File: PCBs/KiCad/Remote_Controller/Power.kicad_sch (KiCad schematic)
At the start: 20 parts

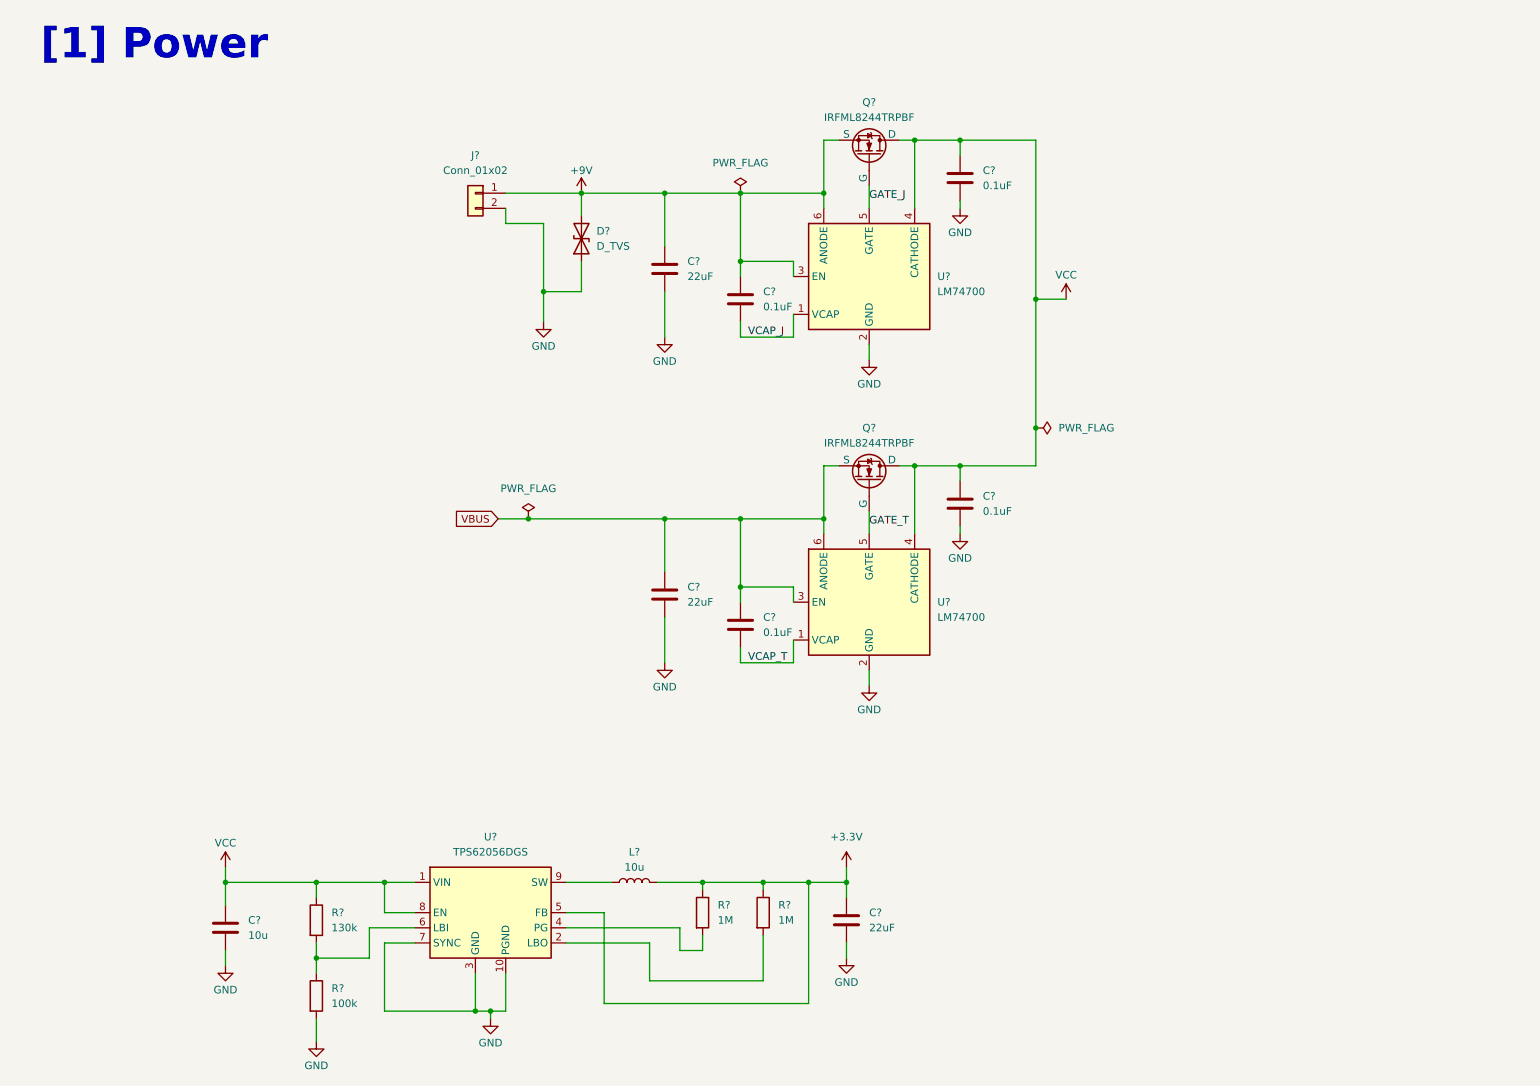
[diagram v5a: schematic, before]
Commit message: Finish power schematic, 3.3V buck converter and 3V LDO
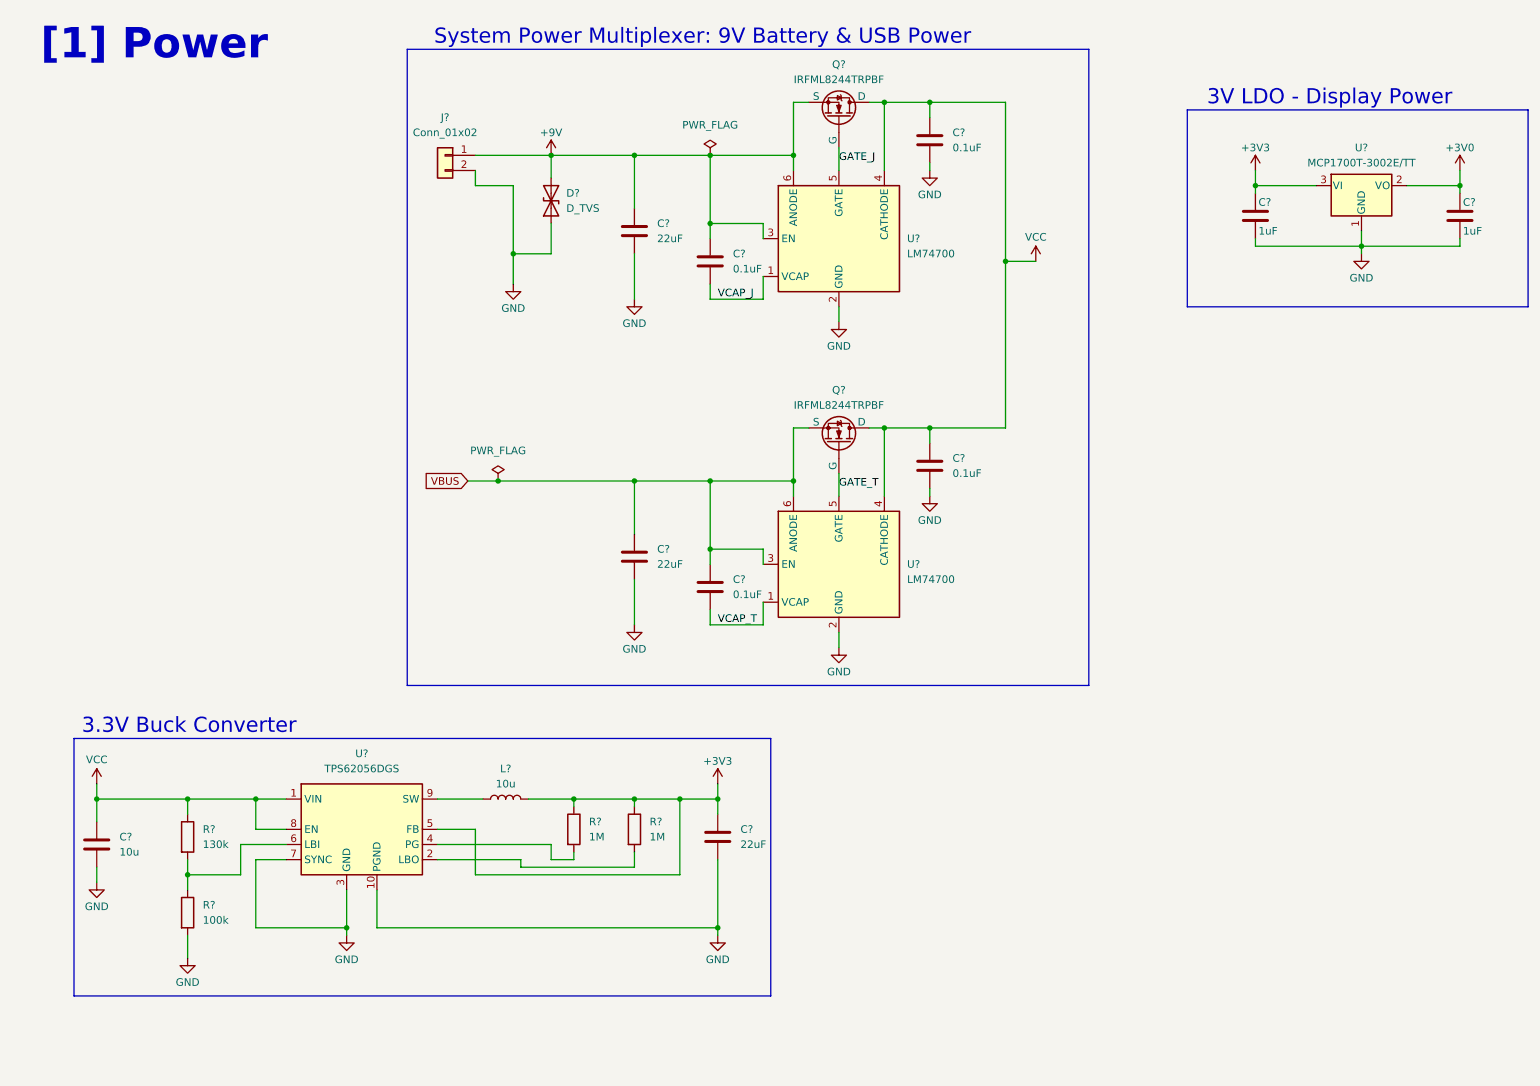
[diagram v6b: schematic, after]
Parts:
- added C? (x2): 1uF, Capacitor_SMD:C_0402_1005Metric, symbol Device:C
- added U?: MCP1700T-3002E/TT, Package_TO_SOT_SMD:SOT-23, symbol Regulator_Linear:MCP1700x-300xxTT
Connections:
- net GND: now also C?.2, C?.2, U?.1 (GND)
- net +3.3V renamed +3V3
- net +3V3: now also C?.1, U?.3 (VI)
- new net +3V0: C?.1, U?.2 (VO)
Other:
- note added: "3.3V Buck Converter"
- note added: "3V LDO - Display Power"
- note added: "System Power Multiplexer: 9V Battery & USB Power"
- moved on the sheet: C?, D?, J?, L?, Q?, R?, U?

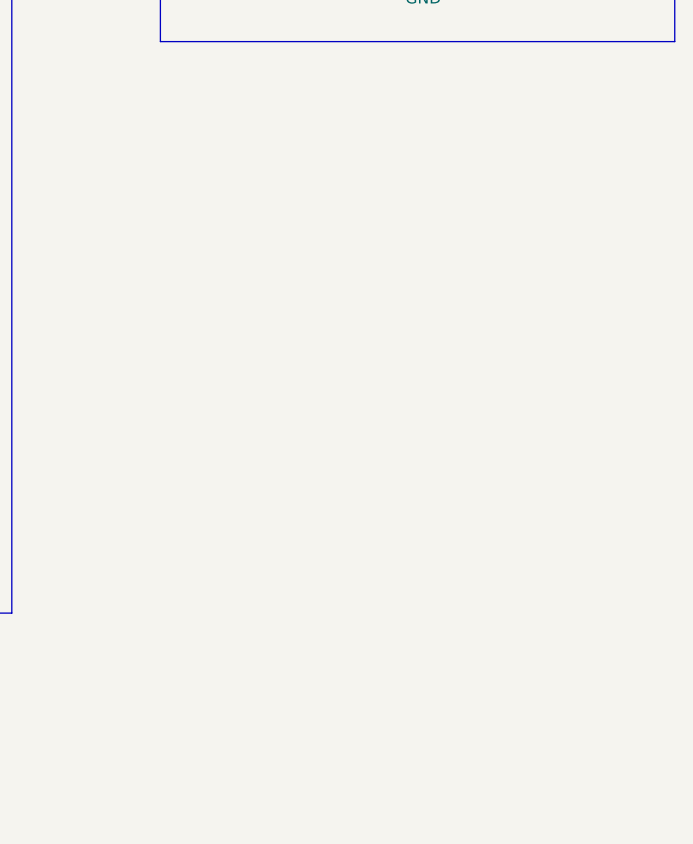
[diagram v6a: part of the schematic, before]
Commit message: Add Power on indicator light, made small corrections
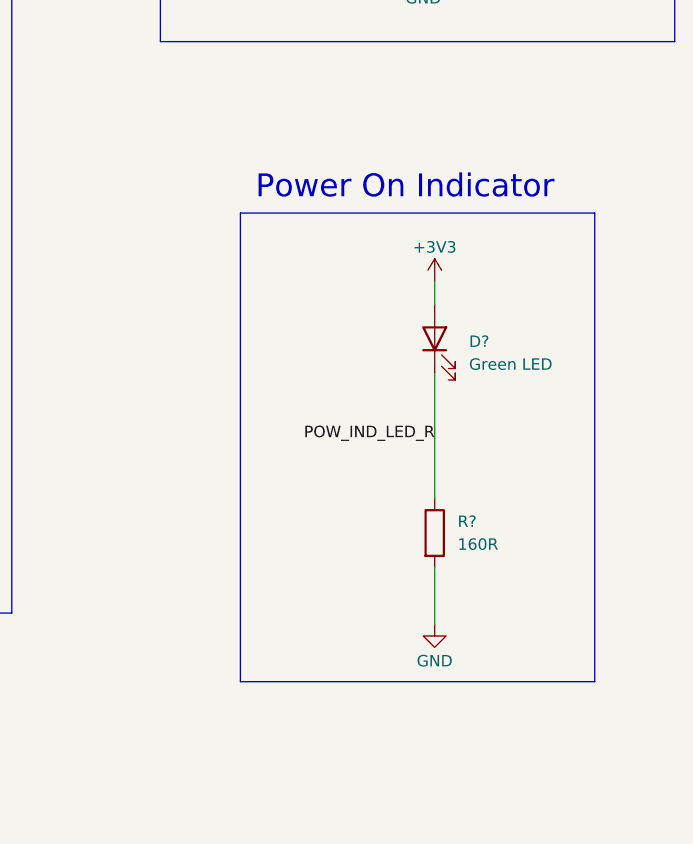
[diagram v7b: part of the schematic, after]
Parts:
- added D?: Green LED, LED_SMD:LED_0603_1608Metric, symbol Device:LED
- added R?: 160R, Resistor_SMD:R_0603_1608Metric, symbol Device:R
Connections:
- net +3V3: now also D?.2 (A)
- net GND: now also R?.2
- new net POW_IND_LED_R: D?.1 (K), R?.1
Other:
- note added: "Power On Indicator"

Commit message: Add power switch
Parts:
- added SW?: Power Switch, symbol Switch:SW_SPST
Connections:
- net +9V: now also SW?.1 (A); no longer C?.1, C?.1, Q?.2 (S), U?.3 (EN), U?.6 (ANODE)
- new net: C?.1, C?.1, Q?.2 (S), SW?.2 (B), U?.3 (EN), U?.6 (ANODE)
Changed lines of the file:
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@@
 	(paper "A4")
 	(junction
-		(at 130.81 170.18)
+		(at 116.84 40.64)
 		(diameter 0)
 		(color 0 0 0 0)
 	)
 	(junction
-		(at 26.67 148.59)
+		(at 130.81 170.18)
 		(diameter 0)
 		(color 0 0 0 0)
 	)
 	(junction
-		(at 143.51 40.64)
+		(at 26.67 148.59)
 		(diameter 0)
 		(color 0 0 0 0)
 	)
 	(junction
-		(at 238.76 55.88)
+		(at 143.51 40.64)
 		(diameter 0)
 		(color 0 0 0 0)
 	)
 	(junction
-		(at 116.84 40.64)
+		(at 238.76 55.88)
 		(diameter 0)
 		(color 0 0 0 0)
@@
 	)
 	(junction
-		(at 102.87 40.64)
-		(diameter 0)
-		(color 0 0 0 0)
-	)
-	(junction
 		(at 106.68 148.59)
 		(diameter 0)
@@
 	)
 	(junction
+		(at 96.52 40.64)
+		(diameter 0)
+		(color 0 0 0 0)
+	)
+	(junction
 		(at 116.84 148.59)
 		(diameter 0)
@@
 	)
 	(junction
+		(at 102.87 40.64)
+		(diameter 0)
+		(color 0 0 0 0)
+	)
+	(junction
 		(at 116.84 95.25)
 		(diameter 0)
@@
 	(wire
 		(pts
-			(xy 102.87 40.64) (xy 116.84 40.64)
-		)
-		(stroke
-			(width 0)
-			(type default)
-		)
-	)
-	(wire
-		(pts
 			(xy 41.91 148.59) (xy 53.34 148.59)
 		)
@@
 	(wire
 		(pts
+			(xy 115.57 40.64) (xy 116.84 40.64)
+		)
+		(stroke
+			(width 0)
+			(type default)
+		)
+	)
+	(wire
+		(pts
 			(xy 231.14 45.72) (xy 220.98 45.72)
 		)
@@
 	(wire
 		(pts
-			(xy 90.17 40.64) (xy 102.87 40.64)
+			(xy 90.17 40.64) (xy 96.52 40.64)
 		)
 		(stroke
@@
 	(wire
 		(pts
+			(xy 102.87 40.64) (xy 105.41 40.64)
+		)
+		(stroke
+			(width 0)
+			(type default)
+		)
+	)
+	(wire
+		(pts
 			(xy 102.87 52.07) (xy 102.87 57.15)
 		)
@@
 	(wire
 		(pts
+			(xy 96.52 40.64) (xy 102.87 40.64)
+		)
+		(stroke
+			(width 0)
+			(type default)
+		)
+	)
+	(wire
+		(pts
 			(xy 220.98 55.88) (xy 238.76 55.88)
 		)
@@
 	(symbol
 		(lib_id "power:+9V")
-		(at 102.87 40.64 0)
+		(at 96.52 40.64 0)
 		(unit 1)
 		(exclude_from_sim no)
@@
 		(dnp no)
 		(property "Reference" "#PWR09"
-			(at 102.87 44.45 0)
+			(at 96.52 44.45 0)
 			(effects
 				(font
@@
 		)
 		(property "Value" "+9V"
-			(at 102.87 36.83 0)
+			(at 96.52 36.83 0)
 			(effects
 				(font
@@
 		)
 		(property "Footprint" ""
-			(at 102.87 40.64 0)
+			(at 96.52 40.64 0)
 			(effects
 				(font
@@
 		)
 		(property "Datasheet" ""
-			(at 102.87 40.64 0)
+			(at 96.52 40.64 0)
 			(effects
 				(font
@@
 		)
 		(property "Description" "Power symbol creates a global label with name \"+9V\""
-			(at 102.87 40.64 0)
+			(at 96.52 40.64 0)
 			(effects
 				(font
@@
 					(unit 1)
 				)
+			)
+		)
+	)
+	(symbol
+		(lib_id "Switch:SW_SPST")
+		(at 110.49 40.64 0)
+		(unit 1)
+		(exclude_from_sim no)
+		(in_bom yes)
+		(on_board yes)
+		(dnp no)
+		(fields_autoplaced yes)
+		(property "Reference" "SW?"
+			(at 110.49 34.29 0)
+			(effects
+				(font
+					(size 1.27 1.27)
+				)
+			)
+		)
+		(property "Value" "Power Switch"
+			(at 110.49 36.83 0)
+			(effects
+				(font
+					(size 1.27 1.27)
+				)
+			)
+		)
+		(property "Footprint" ""
+			(at 110.49 40.64 0)
+			(effects
+				(font
+					(size 1.27 1.27)
+				)
+				(hide yes)
+			)
+		)
+		(property "Datasheet" "~"
+			(at 110.49 40.64 0)
+			(effects
+				(font
+					(size 1.27 1.27)
+				)
+				(hide yes)
+			)
+		)
+		(property "Description" "Single Pole Single Throw (SPST) switch"
+			(at 110.49 40.64 0)
+			(effects
+				(font
+					(size 1.27 1.27)
+				)
+				(hide yes)
+			)
+		)
+		(pin "1"
+		)
+		(pin "2"
+		)
+		(instances
+			(project ""
+				(path "/7afb5074-6b77-4607-a5eb-938c2def45ba/bc757f9b-317d-459c-8896-b31b23ed4983"
+					(reference "SW?")
+					(unit 1)
+				)
